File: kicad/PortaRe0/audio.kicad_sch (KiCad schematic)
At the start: 56 parts, among them J2 SPK_R, J3 SPK_L, J9 PJ-307C, U11 RP2040#2, U13 PCM5102APWR, U14 TPA6132A2RTER, U15 MAX98357AEWL+T_R, U9 MAX98357AEWL+T_L, Y2 C70565

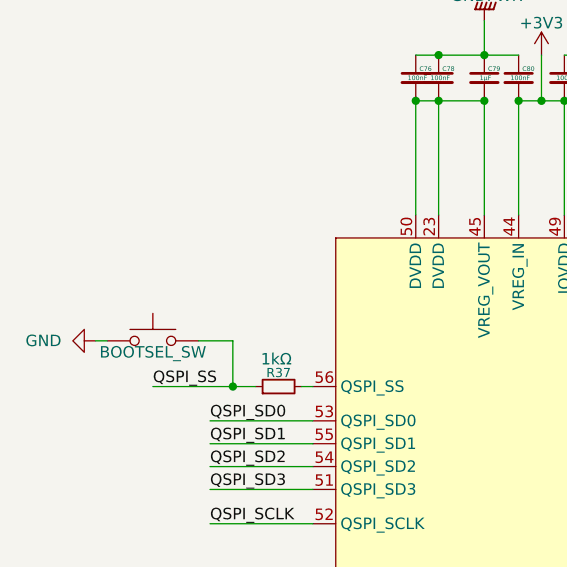
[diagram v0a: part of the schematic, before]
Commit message: Docs: session32終了処理・ドキュメント構成整理・session_close.py作成
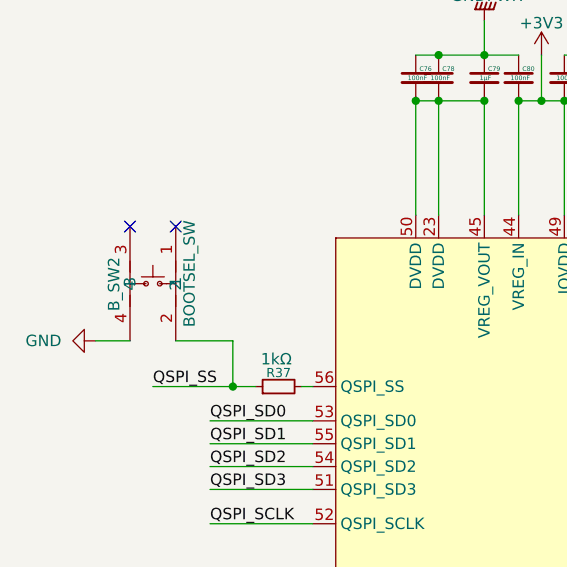
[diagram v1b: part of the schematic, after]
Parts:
- removed K_SW65: BOOTSEL_SW, PortaRe0:KEY-SMD_4P-L4.2-W3.2-P2.20-LS4.6, symbol Switch:SW_Push
- added B_SW2: BOOTSEL_SW, PortaRe0:KEY-SMD_4P-L4.2-W3.2-P2.20-LS4.6, symbol PortaRe0:SKRPABE010
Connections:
- net GND: now also B_SW2.4
- net QSPI_SS: now also B_SW2.2
- no-connect marks 28 -> 30
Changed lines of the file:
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@@
 	)
 	(no_connect
+		(at 41.91 80.01)
+	)
+	(no_connect
 		(at 125.73 134.62)
 	)
@@
 	)
 	(no_connect
+		(at 46.99 80.01)
+	)
+	(no_connect
 		(at 125.73 129.54)
 	)
@@
 	(wire
 		(pts
+			(xy 46.99 92.71) (xy 53.34 92.71)
+		)
+		(stroke
+			(width 0)
+			(type default)
+		)
+	)
+	(wire
+		(pts
 			(xy 252.73 120.65) (xy 243.84 120.65)
 		)
@@
 	(wire
 		(pts
-			(xy 38.1 92.71) (xy 39.37 92.71)
+			(xy 38.1 92.71) (xy 41.91 92.71)
 		)
 		(stroke
@@
 	(wire
 		(pts
-			(xy 49.53 92.71) (xy 53.34 92.71)
-		)
-		(stroke
-			(width 0)
-			(type default)
-		)
-	)
-	(wire
-		(pts
 			(xy 102.87 66.04) (xy 106.68 66.04)
 		)
@@
 	)
 	(symbol
+		(lib_id "PortaRe0:SKRPABE010")
+		(at 44.45 86.36 270)
+		(unit 1)
+		(exclude_from_sim no)
+		(in_bom yes)
+		(on_board yes)
+		(dnp no)
+		(property "Reference" "B_SW2"
+			(at 40.132 89.408 0)
+			(effects
+				(font
+					(size 1.27 1.27)
+				)
+				(justify right)
+			)
+		)
+		(property "Value" "BOOTSEL_SW"
+			(at 48.514 91.186 0)
+			(effects
+				(font
+					(size 1.27 1.27)
+				)
+				(justify right)
+			)
+		)
+		(property "Footprint" "PortaRe0:KEY-SMD_4P-L4.2-W3.2-P2.20-LS4.6"
+			(at 34.29 86.36 0)
+			(effects
+				(font
+					(size 1.27 1.27)
+				)
+				(hide yes)
+			)
+		)
+		(property "Datasheet" "https://lcsc.com/product-detail/Tactile-Switches_ALPS_SKRPABE010_3-2-4-2-2-5-1-57N_C115360.html"
+			(at 31.75 86.36 0)
+			(effects
+				(font
+					(size 1.27 1.27)
+				)
+				(hide yes)
+			)
+		)
+		(property "Description" ""
+			(at 44.45 86.36 0)
+			(effects
+				(font
+					(size 1.27 1.27)
+				)
+				(hide yes)
+			)
+		)
+		(property "LCSC Part" "C115360"
+			(at 29.21 86.36 0)
+			(effects
+				(font
+					(size 1.27 1.27)
+				)
+				(hide yes)
+			)
+		)
+		(pin "4"
+		)
+		(pin "3"
+		)
+		(pin "2"
+		)
+		(pin "1"
+		)
+		(instances
+			(project "PortaRe0"
+				(path "/479aadc4-f9a0-4ec2-b000-6a17237038f1/6f018b3a-f554-45a0-adb8-bf1e4994a5d2"
+					(reference "B_SW2")
+					(unit 1)
+				)
+			)
+		)
+	)
+	(symbol
 		(lib_id "power:GNDPWR")
 		(at 212.09 140.97 270)
@@
 					(unit 1)
 				)
-			)
-		)
-	)
-	(symbol
-		(lib_id "Switch:SW_Push")
-		(at 44.45 92.71 0)
-		(unit 1)
-		(exclude_from_sim no)
-		(in_bom yes)
-		(on_board yes)
-		(dnp no)
-		(property "Reference" "K_SW65"
-			(at 44.45 95.758 0)
-			(effects
-				(font
-					(size 1.27 1.27)
-				)
-				(hide yes)
-			)
-		)
-		(property "Value" "BOOTSEL_SW"
-			(at 44.45 93.98 0)
-			(effects
-				(font
-					(size 1.27 1.27)
-				)
-			)
-		)
-		(property "Footprint" "PortaRe0:KEY-SMD_4P-L4.2-W3.2-P2.20-LS4.6"
-			(at 44.45 87.63 0)
-			(effects
-				(font
-					(size 1.27 1.27)
-				)
-				(hide yes)
-			)
-		)
-		(property "Datasheet" "~"
-			(at 44.45 87.63 0)
-			(effects
-				(font
-					(size 1.27 1.27)
-				)
-				(hide yes)
-			)
-		)
-		(property "Description" "Push button switch, generic, two pins"
-			(at 44.45 92.71 0)
-			(effects
-				(font
-					(size 1.27 1.27)
-				)
-				(hide yes)
-			)
-		)
-		(pin "2"
-		)
-		(pin "1"
-		)
-		(instances
-			(project "PortaRe0"
-				(path "/479aadc4-f9a0-4ec2-b000-6a17237038f1/6f018b3a-f554-45a0-adb8-bf1e4994a5d2"
-					(reference "K_SW65")
-					(unit 1)
-				)

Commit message: Docs: session34終了処理・0402化確定・ディスプレイ調査・PCBレイアウト進行中
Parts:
- C115, C116, C117, C118, C119, C71, C72, C74, C75, C76, C77, C78, C79, C80, C81, C82, C83, C84, C85, C86, C87, C88, C89, C90, C91, C92, C93, C94, C95, C96, C97, C98, C99: footprint Capacitor_SMD:C_0603_1608Metric -> Capacitor_SMD:C_0402_1005Metric
- R36, R37, R38, R39, R54, R63, R8: footprint Resistor_SMD:R_0603_1608Metric -> Resistor_SMD:R_0402_1005Metric
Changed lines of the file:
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@@
 			)
 		)
-		(property "Footprint" "Capacitor_SMD:C_0603_1608Metric"
+		(property "Footprint" "Capacitor_SMD:C_0402_1005Metric"
 			(at 176.53 63.5 0)
 			(effects
@@
 			)
 		)
-		(property "Footprint" "Capacitor_SMD:C_0603_1608Metric"
+		(property "Footprint" "Capacitor_SMD:C_0402_1005Metric"
 			(at 210.82 153.67 0)
 			(effects
@@
 			)
 		)
-		(property "Footprint" "Capacitor_SMD:C_0603_1608Metric"
+		(property "Footprint" "Capacitor_SMD:C_0402_1005Metric"
 			(at 271.78 153.67 0)
 			(effects
@@
 			)
 		)
-		(property "Footprint" "Capacitor_SMD:C_0603_1608Metric"
+		(property "Footprint" "Capacitor_SMD:C_0402_1005Metric"
 			(at 114.3 72.39 0)
 			(effects
@@
 			)
 		)
-		(property "Footprint" "Capacitor_SMD:C_0603_1608Metric"
+		(property "Footprint" "Capacitor_SMD:C_0402_1005Metric"
 			(at 97.79 63.5 0)
 			(effects
@@
 			)
 		)
-		(property "Footprint" "Capacitor_SMD:C_0603_1608Metric"
+		(property "Footprint" "Capacitor_SMD:C_0402_1005Metric"
 			(at 190.5 125.73 0)
 			(effects
@@
 			)
 		)
-		(property "Footprint" "Capacitor_SMD:C_0603_1608Metric"
+		(property "Footprint" "Capacitor_SMD:C_0402_1005Metric"
 			(at 92.71 63.5 0)
 			(effects
@@
 			)
 		)
-		(property "Footprint" "Capacitor_SMD:C_0603_1608Metric"
+		(property "Footprint" "Capacitor_SMD:C_0402_1005Metric"
 			(at 252.73 123.19 0)
 			(effects
@@
 			)
 		)
-		(property "Footprint" "Capacitor_SMD:C_0603_1608Metric"
+		(property "Footprint" "Capacitor_SMD:C_0402_1005Metric"
 			(at 95.25 63.5 0)
 			(effects
@@
 			)
 		)
-		(property "Footprint" "Capacitor_SMD:C_0603_1608Metric"
+		(property "Footprint" "Capacitor_SMD:C_0402_1005Metric"
 			(at 190.5 143.51 0)
 			(effects
@@
 			)
 		)
-		(property "Footprint" "Capacitor_SMD:C_0603_1608Metric"
+		(property "Footprint" "Capacitor_SMD:C_0402_1005Metric"
 			(at 48.26 137.16 0)
 			(effects
@@
 			)
 		)
-		(property "Footprint" "Capacitor_SMD:C_0603_1608Metric"
+		(property "Footprint" "Capacitor_SMD:C_0402_1005Metric"
 			(at 76.2 63.5 0)
 			(effects
@@
 			)
 		)
-		(property "Footprint" "Resistor_SMD:R_0603_1608Metric"
+		(property "Footprint" "Resistor_SMD:R_0402_1005Metric"
 			(at 54.61 149.86 0)
 			(effects
@@
 			)
 		)
-		(property "Footprint" "Capacitor_SMD:C_0603_1608Metric"
+		(property "Footprint" "Capacitor_SMD:C_0402_1005Metric"
 			(at 187.96 91.44 0)
 			(effects
@@
 			)
 		)
-		(property "Footprint" "Capacitor_SMD:C_0603_1608Metric"
+		(property "Footprint" "Capacitor_SMD:C_0402_1005Metric"
 			(at 210.82 161.29 0)
 			(effects
@@
 			)
 		)
-		(property "Footprint" "Capacitor_SMD:C_0603_1608Metric"
+		(property "Footprint" "Capacitor_SMD:C_0402_1005Metric"
 			(at 106.68 63.5 0)
 			(effects
@@
 			)
 		)
-		(property "Footprint" "Capacitor_SMD:C_0603_1608Metric"
+		(property "Footprint" "Capacitor_SMD:C_0402_1005Metric"
 			(at 190.5 121.92 0)
 			(effects
@@
 			)
 		)
-		(property "Footprint" "Resistor_SMD:R_0603_1608Metric"
+		(property "Footprint" "Resistor_SMD:R_0402_1005Metric"
 			(at 137.16 114.3 0)
 			(effects
@@
 			)
 		)
-		(property "Footprint" "Resistor_SMD:R_0603_1608Metric"
+		(property "Footprint" "Resistor_SMD:R_0402_1005Metric"
 			(at 204.47 156.21 0)
 			(effects
@@
 			)
 		)
-		(property "Footprint" "Capacitor_SMD:C_0603_1608Metric"
+		(property "Footprint" "Capacitor_SMD:C_0402_1005Metric"
 			(at 190.5 139.7 0)
 			(effects
@@
 			)
 		)
-		(property "Footprint" "Capacitor_SMD:C_0603_1608Metric"
+		(property "Footprint" "Capacitor_SMD:C_0402_1005Metric"
 			(at 271.78 166.37 0)
 			(effects
@@
 			)
 		)
-		(property "Footprint" "Capacitor_SMD:C_0603_1608Metric"
+		(property "Footprint" "Capacitor_SMD:C_0402_1005Metric"
 			(at 215.9 128.27 0)
 			(effects
@@
 			)
 		)
-		(property "Footprint" "Capacitor_SMD:C_0603_1608Metric"
+		(property "Footprint" "Capacitor_SMD:C_0402_1005Metric"
 			(at 102.87 63.5 0)
 			(effects
@@
 			)
 		)
-		(property "Footprint" "Capacitor_SMD:C_0603_1608Metric"
+		(property "Footprint" "Capacitor_SMD:C_0402_1005Metric"
 			(at 259.08 171.45 0)
 			(effects
@@
 			)
 		)
-		(property "Footprint" "Capacitor_SMD:C_0603_1608Metric"
+		(property "Footprint" "Capacitor_SMD:C_0402_1005Metric"
 			(at 48.26 132.08 0)
 			(effects
@@
 			)
 		)
-		(property "Footprint" "Capacitor_SMD:C_0603_1608Metric"
+		(property "Footprint" "Capacitor_SMD:C_0402_1005Metric"
 			(at 73.66 63.5 0)
 			(effects
@@
 			)
 		)
-		(property "Footprint" "Capacitor_SMD:C_0603_1608Metric"
+		(property "Footprint" "Capacitor_SMD:C_0402_1005Metric"
 			(at 271.78 121.92 0)
 			(effects
@@
 			)
 		)
-		(property "Footprint" "Capacitor_SMD:C_0603_1608Metric"
+		(property "Footprint" "Capacitor_SMD:C_0402_1005Metric"
 			(at 81.28 63.5 0)
 			(effects
@@
 			)
 		)
-		(property "Footprint" "Resistor_SMD:R_0603_1608Metric"
+		(property "Footprint" "Resistor_SMD:R_0402_1005Metric"
 			(at 110.49 72.39 0)
 			(effects
@@
 			)
 		)
-		(property "Footprint" "Capacitor_SMD:C_0603_1608Metric"
+		(property "Footprint" "Capacitor_SMD:C_0402_1005Metric"
 			(at 271.78 157.48 0)
 			(effects
@@
 			)
 		)
-		(property "Footprint" "Capacitor_SMD:C_0603_1608Metric"
+		(property "Footprint" "Capacitor_SMD:C_0402_1005Metric"
 			(at 100.33 63.5 0)
 			(effects
@@
 			)
 		)
-		(property "Footprint" "Resistor_SMD:R_0603_1608Metric"
+		(property "Footprint" "Resistor_SMD:R_0402_1005Metric"
 			(at 113.03 44.45 0)
 			(effects
@@
 			)
 		)
-		(property "Footprint" "Resistor_SMD:R_0603_1608Metric"
+		(property "Footprint" "Resistor_SMD:R_0402_1005Metric"
 			(at 58.42 97.79 0)
 			(effects
@@
 			)
 		)
-		(property "Footprint" "Capacitor_SMD:C_0603_1608Metric"
+		(property "Footprint" "Capacitor_SMD:C_0402_1005Metric"
 			(at 85.09 63.5 0)
 			(effects
@@
 			)
 		)
-		(property "Footprint" "Capacitor_SMD:C_0603_1608Metric"
+		(property "Footprint" "Capacitor_SMD:C_0402_1005Metric"
 			(at 76.2 41.91 0)
 			(effects
@@
 			)
 		)
-		(property "Footprint" "Resistor_SMD:R_0603_1608Metric"
+		(property "Footprint" "Resistor_SMD:R_0402_1005Metric"
 			(at 204.47 163.83 0)
 			(effects
@@
 			)
 		)
-		(property "Footprint" "Capacitor_SMD:C_0603_1608Metric"
+		(property "Footprint" "Capacitor_SMD:C_0402_1005Metric"
 			(at 203.2 123.19 0)
 			(effects
@@
 			)
 		)
-		(property "Footprint" "Capacitor_SMD:C_0603_1608Metric"
+		(property "Footprint" "Capacitor_SMD:C_0402_1005Metric"
 			(at 271.78 125.73 0)
 			(effects
@@
 			)
 		)
-		(property "Footprint" "Capacitor_SMD:C_0603_1608Metric"
+		(property "Footprint" "Capacitor_SMD:C_0402_1005Metric"
 			(at 209.55 173.99 0)
 			(effects
@@
 			)
 		)
-		(property "Footprint" "Capacitor_SMD:C_0603_1608Metric"
+		(property "Footprint" "Capacitor_SMD:C_0402_1005Metric"
 			(at 90.17 63.5 0)
 			(effects
